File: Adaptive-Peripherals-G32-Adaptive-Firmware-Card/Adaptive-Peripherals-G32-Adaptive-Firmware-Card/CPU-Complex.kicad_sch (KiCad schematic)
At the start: 22 parts, among them Q7 MPS3646, U10 74LS32, U11 CAT71C256L-85, U12 74LS11, U14 74LS373, U15 74HCTLS245, U16 74HCTLS374, U18 74HCTLS00, U19 74LS175, U21 74HCTLS245, U22 74HCTLS00, U23 74HCTLS00, U24 74HCTLS245, U26 74HCTLS00, U6 74LS138, U8 65SC816-4, U9 74HCTLS04

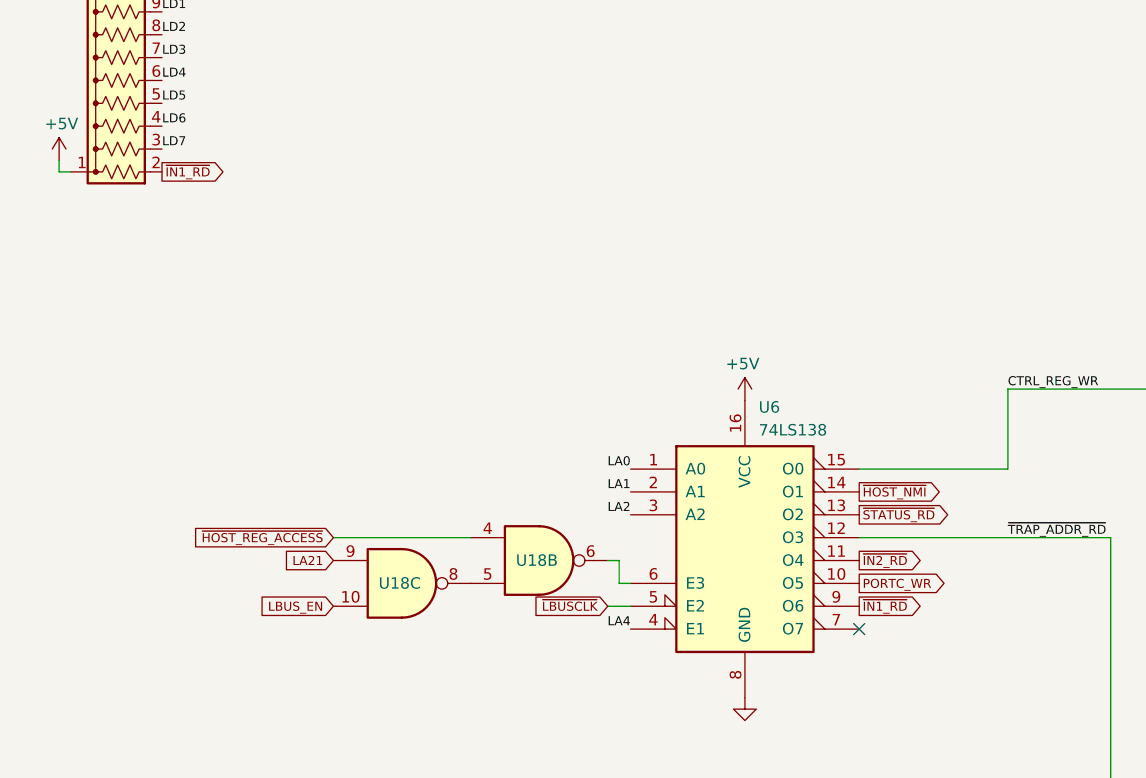
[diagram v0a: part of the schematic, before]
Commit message: Add breakout box information for the Adaptive Peripherals card
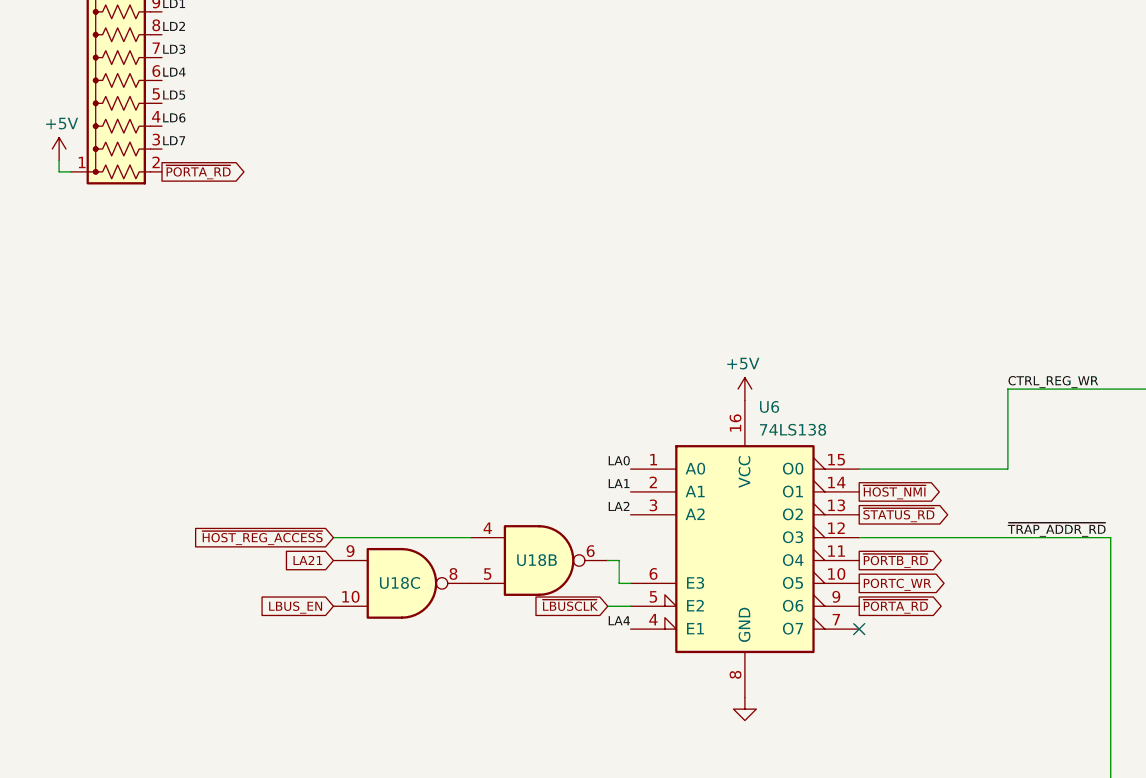
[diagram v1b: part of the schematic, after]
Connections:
- net ~{IN1_RD} renamed ~{PORTA_RD}
- net ~{IN2_RD} renamed ~{PORTB_RD}
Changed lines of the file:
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@@
 	(title_block
 		(title "Adaptive Peripherals G32 Adaptive Firmware Card")
-		(date "2024-04-02")
+		(date "2024-11-14")
 		(rev "D")
 		(comment 2 "captured by Mark Aikens")
@@
 		)
 	)
-	(global_label "~{IN2_RD}"
+	(global_label "~{PORTB_RD}"
 		(shape output)
 		(at 189.23 204.47 0)
@@
 		)
 	)
-	(global_label "~{IN1_RD}"
+	(global_label "~{PORTA_RD}"
 		(shape output)
 		(at 189.23 209.55 0)
@@
 		)
 	)
-	(global_label "~{IN1_RD}"
+	(global_label "~{PORTA_RD}"
 		(shape output)
 		(at 111.76 161.29 0)
